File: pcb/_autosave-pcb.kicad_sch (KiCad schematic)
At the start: 20 parts, among them J1 Conn_01x04_MountingPin, J2 Conn_01x04_MountingPin, J4 Conn_ARM_SWD_TagConnect_TC203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, U1 THVD1451, U2 STM32G0B1KBUx, U3 AP2210

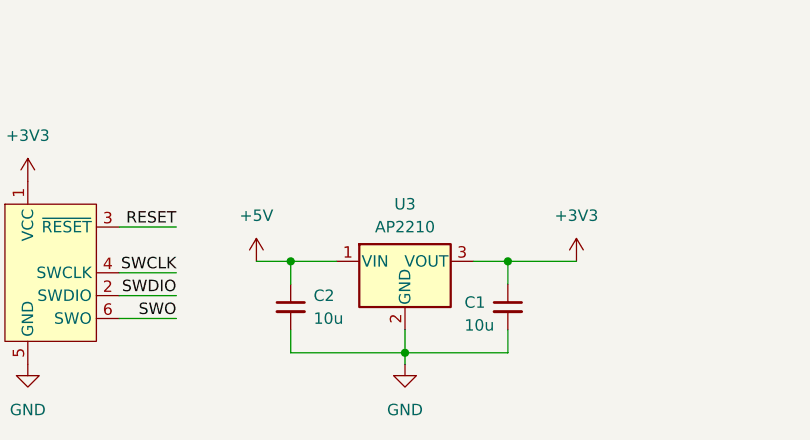
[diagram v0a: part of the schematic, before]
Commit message: add rs485
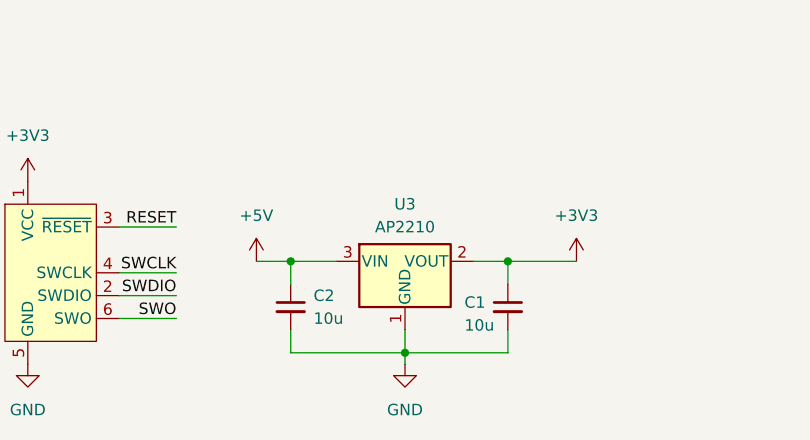
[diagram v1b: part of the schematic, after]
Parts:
- LS1: footprint goatworks-footprint-library:OWR-061220LA-32 -> goatworks-footprint-library:PKMCS0909E4000-R1
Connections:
- net +3V3: now also U3.2 (VOUT); no longer U3.3 (VOUT)
- net +5V: now also U3.3 (VIN); no longer U3.1 (VIN)
- net GND: now also U3.1 (GND); no longer U3.2 (GND)
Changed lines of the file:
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@@
 			)
 		)
-		(property "Footprint" "goatworks-footprint-library:OWR-061220LA-32"
+		(property "Footprint" "goatworks-footprint-library:PKMCS0909E4000-R1"
 			(at 152.019 130.81 0)
 			(effects
